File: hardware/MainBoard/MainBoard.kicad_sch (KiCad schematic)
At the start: 29 parts, among them J1 Conn_02x16_Top_Bottom, J2 Conn_02x16_Top_Bottom, J7 Conn_02x16_Top_Bottom, Q2 FDN340P, Q3 FDN340P, U1 ESP32-S3-WROOM-1, U2 AMS1117-3.3, U3 AMS1117-5.0, U4 TPS22917DBV, U5 TPS22917DBV

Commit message: sanity checked, ready for production
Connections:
- net +5V renamed PWR_SELECT
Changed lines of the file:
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@@
 	(wire
 		(pts
-			(xy 58.42 29.21) (xy 58.42 30.48)
+			(xy 55.88 25.4) (xy 55.88 26.67)
 		)
 		(stroke
@@
 	(wire
 		(pts
-			(xy 58.42 30.48) (xy 57.15 30.48)
+			(xy 55.88 26.67) (xy 54.61 26.67)
 		)
 		(stroke
@@
 		)
 	)
+	(global_label "PWR_SELECT"
+		(shape input)
+		(at 83.82 38.1 0)
+		(fields_autoplaced yes)
+		(effects
+			(font
+				(size 0.762 0.762)
+			)
+			(justify left)
+		)
+		(property "Intersheetrefs" "${INTERSHEET_REFS}"
+			(at 92.6509 38.1 0)
+			(effects
+				(font
+					(size 1.27 1.27)
+				)
+				(justify left)
+				(hide yes)
+			)
+		)
+	)
 	(global_label "SD_DET"
 		(shape bidirectional)
@@
 		)
 	)
+	(global_label "PWR_SELECT"
+		(shape input)
+		(at 46.99 31.75 0)
+		(fields_autoplaced yes)
+		(effects
+			(font
+				(size 0.762 0.762)
+			)
+			(justify left)
+		)
+		(property "Intersheetrefs" "${INTERSHEET_REFS}"
+			(at 55.8209 31.75 0)
+			(effects
+				(font
+					(size 1.27 1.27)
+				)
+				(justify left)
+				(hide yes)
+			)
+		)
+	)
 	(global_label "CONN_13"
 		(shape bidirectional)
@@
 		)
 	)
+	(global_label "PWR_SELECT"
+		(shape input)
+		(at 55.88 46.99 0)
+		(fields_autoplaced yes)
+		(effects
+			(font
+				(size 0.762 0.762)
+			)
+			(justify left)
+		)
+		(property "Intersheetrefs" "${INTERSHEET_REFS}"
+			(at 64.7109 46.99 0)
+			(effects
+				(font
+					(size 1.27 1.27)
+				)
+				(justify left)
+				(hide yes)
+			)
+		)
+	)
 	(global_label "CONN_14"
 		(shape bidirectional)
@@
 	(global_label "VBUS"
 		(shape input)
-		(at 57.15 30.48 180)
+		(at 54.61 26.67 180)
 		(fields_autoplaced yes)
 		(effects
@@
 		)
 		(property "Intersheetrefs" "${INTERSHEET_REFS}"
-			(at 52.4195 30.48 0)
+			(at 49.8795 26.67 0)
 			(effects
 				(font
@@
 	)
 	(symbol
-		(lib_id "power:+5V")
-		(at 55.88 41.91 270)
-		(unit 1)
-		(exclude_from_sim no)
-		(in_bom yes)
-		(on_board yes)
-		(dnp no)
-		(fields_autoplaced yes)
-		(property "Reference" "#PWR025"
-			(at 52.07 41.91 0)
-			(effects
-				(font
-					(size 1.27 1.27)
-				)
-				(hide yes)
-			)
-		)
-		(property "Value" "+5V"
-			(at 59.69 41.9099 90)
-			(effects
-				(font
-					(size 1.27 1.27)
-				)
-				(justify left)
-			)
-		)
-		(property "Footprint" ""
-			(at 55.88 41.91 0)
-			(effects
-				(font
-					(size 1.27 1.27)
-				)
-				(hide yes)
-			)
-		)
-		(property "Datasheet" ""
-			(at 55.88 41.91 0)
-			(effects
-				(font
-					(size 1.27 1.27)
-				)
-				(hide yes)
-			)
-		)
-		(property "Description" "Power symbol creates a global label with name \"+5V\""
-			(at 55.88 41.91 0)
-			(effects
-				(font
-					(size 1.27 1.27)
-				)
-				(hide yes)
-			)
-		)
-		(pin "1"
-		)
-		(instances
-			(project "MainBoard"
-				(path "/988df97c-fca1-40e2-af98-331e3f3f354f"
-					(reference "#PWR025")
-					(unit 1)
-				)
-			)
-		)
-	)
-	(symbol
 		(lib_id "Connector_Generic:Conn_01x01")
 		(at 165.1 111.76 0)
@@
 	)
 	(symbol
-		(lib_id "power:+5V")
-		(at 46.99 31.75 0)
-		(unit 1)
-		(exclude_from_sim no)
-		(in_bom yes)
-		(on_board yes)
-		(dnp no)
-		(fields_autoplaced yes)
-		(property "Reference" "#PWR022"
-			(at 46.99 35.56 0)
-			(effects
-				(font
-					(size 1.27 1.27)
-				)
-				(hide yes)
-			)
-		)
-		(property "Value" "+5V"
-			(at 46.99 26.67 0)
-			(effects
-				(font
-					(size 1.27 1.27)
-				)
-			)
-		)
-		(property "Footprint" ""
-			(at 46.99 31.75 0)
-			(effects
-				(font
-					(size 1.27 1.27)
-				)
-				(hide yes)
-			)
-		)
-		(property "Datasheet" ""
-			(at 46.99 31.75 0)
-			(effects
-				(font
-					(size 1.27 1.27)
-				)
-				(hide yes)
-			)
-		)
-		(property "Description" "Power symbol creates a global label with name \"+5V\""
-			(at 46.99 31.75 0)
-			(effects
-				(font
-					(size 1.27 1.27)
-				)
-				(hide yes)
-			)
-		)
-		(pin "1"
-		)
-		(instances
-			(project ""
-				(path "/988df97c-fca1-40e2-af98-331e3f3f354f"
-					(reference "#PWR022")
-					(unit 1)
-				)
-			)
-		)
-	)
-	(symbol
 		(lib_id "Device:C_Small")
 		(at 111.76 69.85 0)
@@
 	)
 	(symbol
-		(lib_id "power:+5V")
-		(at 83.82 38.1 180)
-		(unit 1)
-		(exclude_from_sim no)
-		(in_bom yes)
-		(on_board yes)
-		(dnp no)
-		(fields_autoplaced yes)
-		(property "Reference" "#PWR023"
-			(at 83.82 34.29 0)
-			(effects
-				(font
-					(size 1.27 1.27)
-				)
-				(hide yes)
-			)
-		)
-		(property "Value" "+5V"
-			(at 83.82 43.18 0)
-			(effects
-				(font
-					(size 1.27 1.27)
-				)
-			)
-		)
-		(property "Footprint" ""
-			(at 83.82 38.1 0)
-			(effects
-				(font
-					(size 1.27 1.27)
-				)
-				(hide yes)
-			)
-		)
-		(property "Datasheet" ""
-			(at 83.82 38.1 0)
-			(effects
-				(font
-					(size 1.27 1.27)
-				)
-				(hide yes)
-			)
-		)
-		(property "Description" "Power symbol creates a global label with name \"+5V\""
-			(at 83.82 38.1 0)
-			(effects
-				(font
-					(size 1.27 1.27)
-				)
-				(hide yes)
-			)
-		)
-		(pin "1"
-		)
-		(instances
-			(project ""
-				(path "/988df97c-fca1-40e2-af98-331e3f3f354f"
-					(reference "#PWR023")
-					(unit 1)
-				)
-			)
-		)
-	)
-	(symbol
 		(lib_id "Device:C_Small")
 		(at 116.84 69.85 0)
@@
 	(symbol
 		(lib_id "power:PWR_FLAG")
-		(at 55.88 41.91 0)
+		(at 55.88 46.99 0)
 		(unit 1)
 		(exclude_from_sim no)
@@
 		(fields_autoplaced yes)
 		(property "Reference" "#FLG05"
-			(at 55.88 40.005 0)
+			(at 55.88 45.085 0)
 			(effects
 				(font
@@
 		)
 		(property "Value" "PWR_FLAG"
-			(at 55.88 36.83 0)
+			(at 55.88 41.91 0)
 			(effects
 				(font
@@
 		)
 		(property "Footprint" ""
-			(at 55.88 41.91 0)
+			(at 55.88 46.99 0)
 			(effects
 				(font
@@
 		)
 		(property "Datasheet" "~"
-			(at 55.88 41.91 0)
+			(at 55.88 46.99 0)
 			(effects
 				(font
@@
 		)
 		(property "Description" "Special symbol for telling ERC where power comes from"
-			(at 55.88 41.91 0)
+			(at 55.88 46.99 0)
 			(effects
 				(font
@@
 	(symbol
 		(lib_id "power:PWR_FLAG")
-		(at 58.42 29.21 0)
+		(at 55.88 25.4 0)
 		(unit 1)
 		(exclude_from_sim no)
@@
 		(fields_autoplaced yes)
 		(property "Reference" "#FLG03"
-			(at 58.42 27.305 0)
+			(at 55.88 23.495 0)
 			(effects
 				(font
@@
 		)
 		(property "Value" "PWR_FLAG"
-			(at 58.42 24.13 0)
+			(at 55.88 20.32 0)
 			(effects
 				(font
@@
 		)
 		(property "Footprint" ""
-			(at 58.42 29.21 0)
+			(at 55.88 25.4 0)
 			(effects
 				(font
@@
 		)
 		(property "Datasheet" "~"
-			(at 58.42 29.21 0)
+			(at 55.88 25.4 0)
 			(effects
 				(font
@@
 		)
 		(property "Description" "Special symbol for telling ERC where power comes from"
-			(at 58.42 29.21 0)
+			(at 55.88 25.4 0)
 			(effects
 				(font

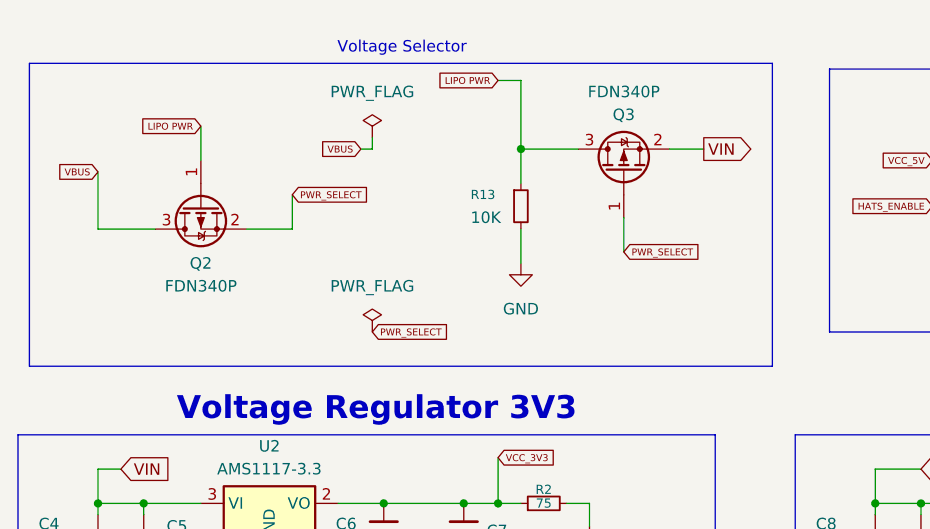
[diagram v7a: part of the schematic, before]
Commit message: changed voltage selector to actually work
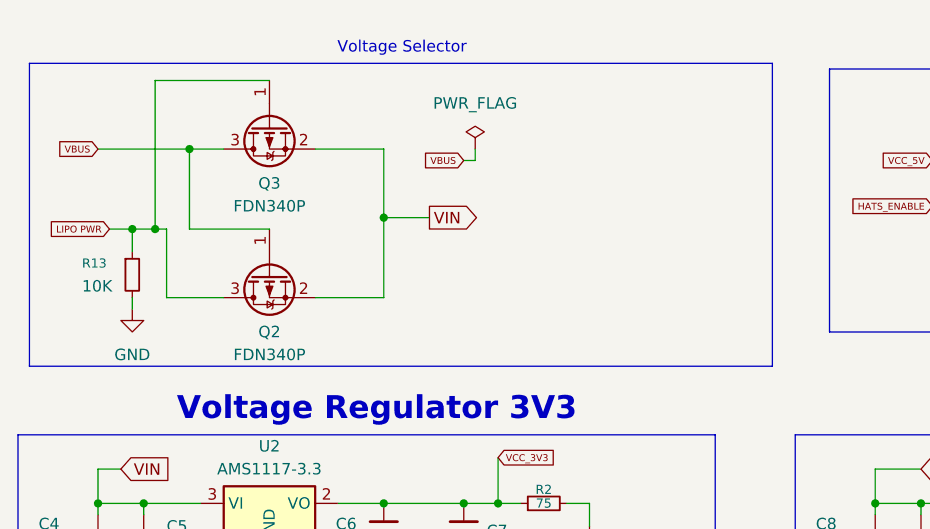
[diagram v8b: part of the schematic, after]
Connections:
- net CONN_21: now also Q2.2 (S)
- net LIPO PWR: now also Q2.3 (D), Q3.1 (G); no longer Q2.1 (G), Q3.3 (D)
- net VBUS: now also Q2.1 (G), Q3.3 (D); no longer Q2.3 (D)
- removed net PWR_SELECT: Q2.2 (S), Q3.1 (G)
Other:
- moved on the sheet: Q2, Q3, R13
